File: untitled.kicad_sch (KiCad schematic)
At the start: 19 parts, among them J4 EURO_PWR, U2 AP2204K-3.3, U3 LM1117-5.0, U4 LM4040DBZ-5

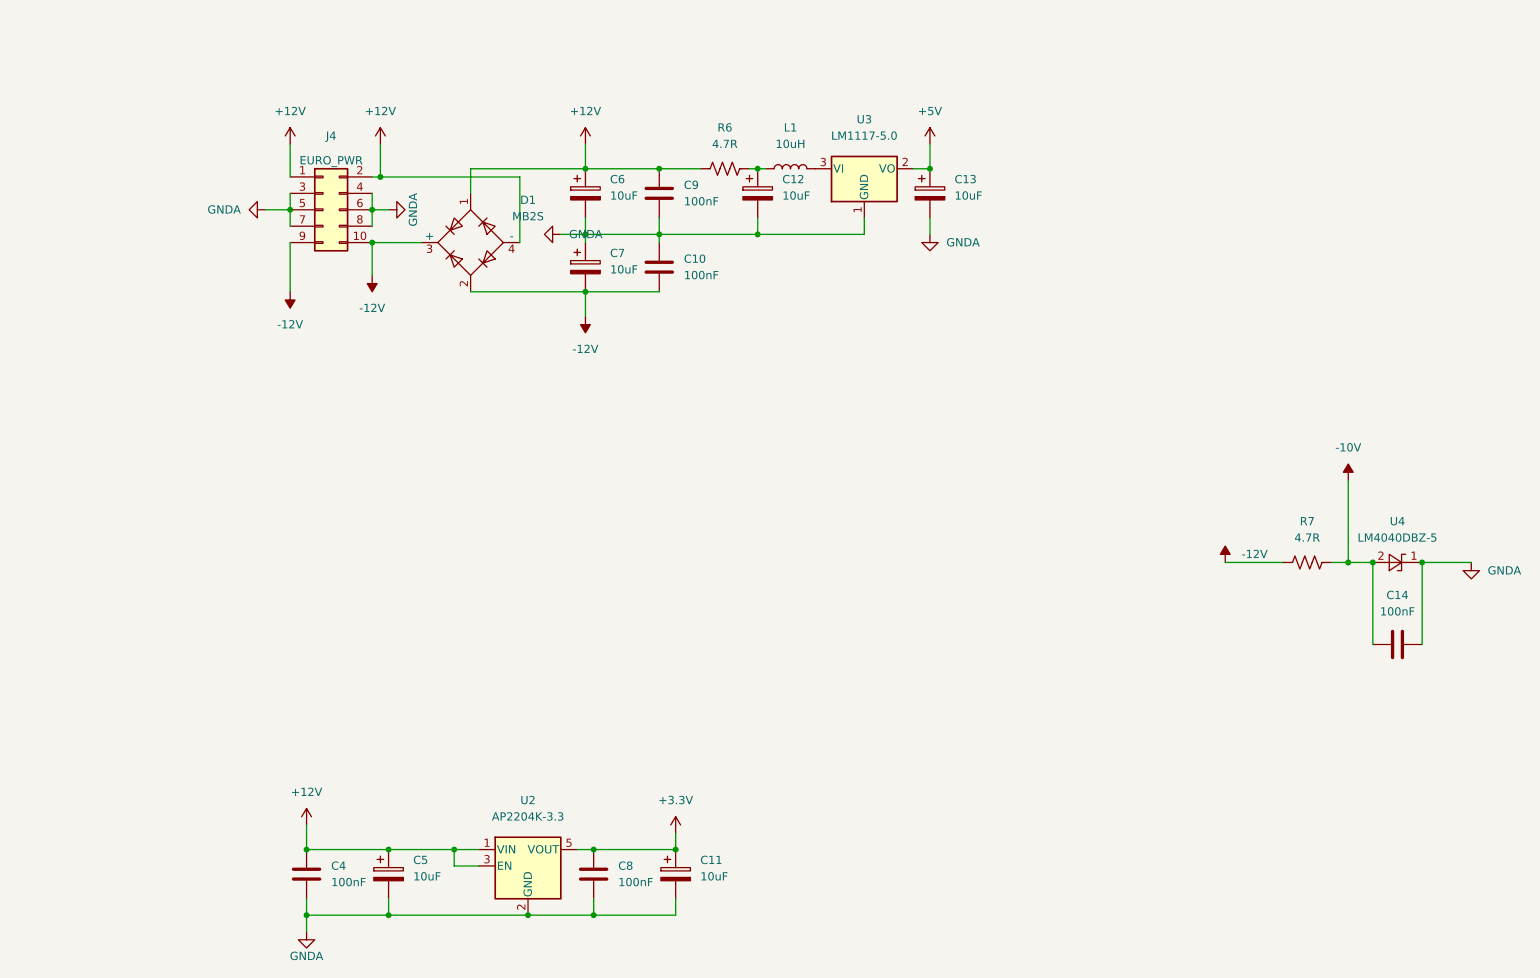
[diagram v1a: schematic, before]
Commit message: Version update
Added DC/DC power block and opAmps for audio input. Redesigned PCB completely moving all components to one side so that it can lay flat.
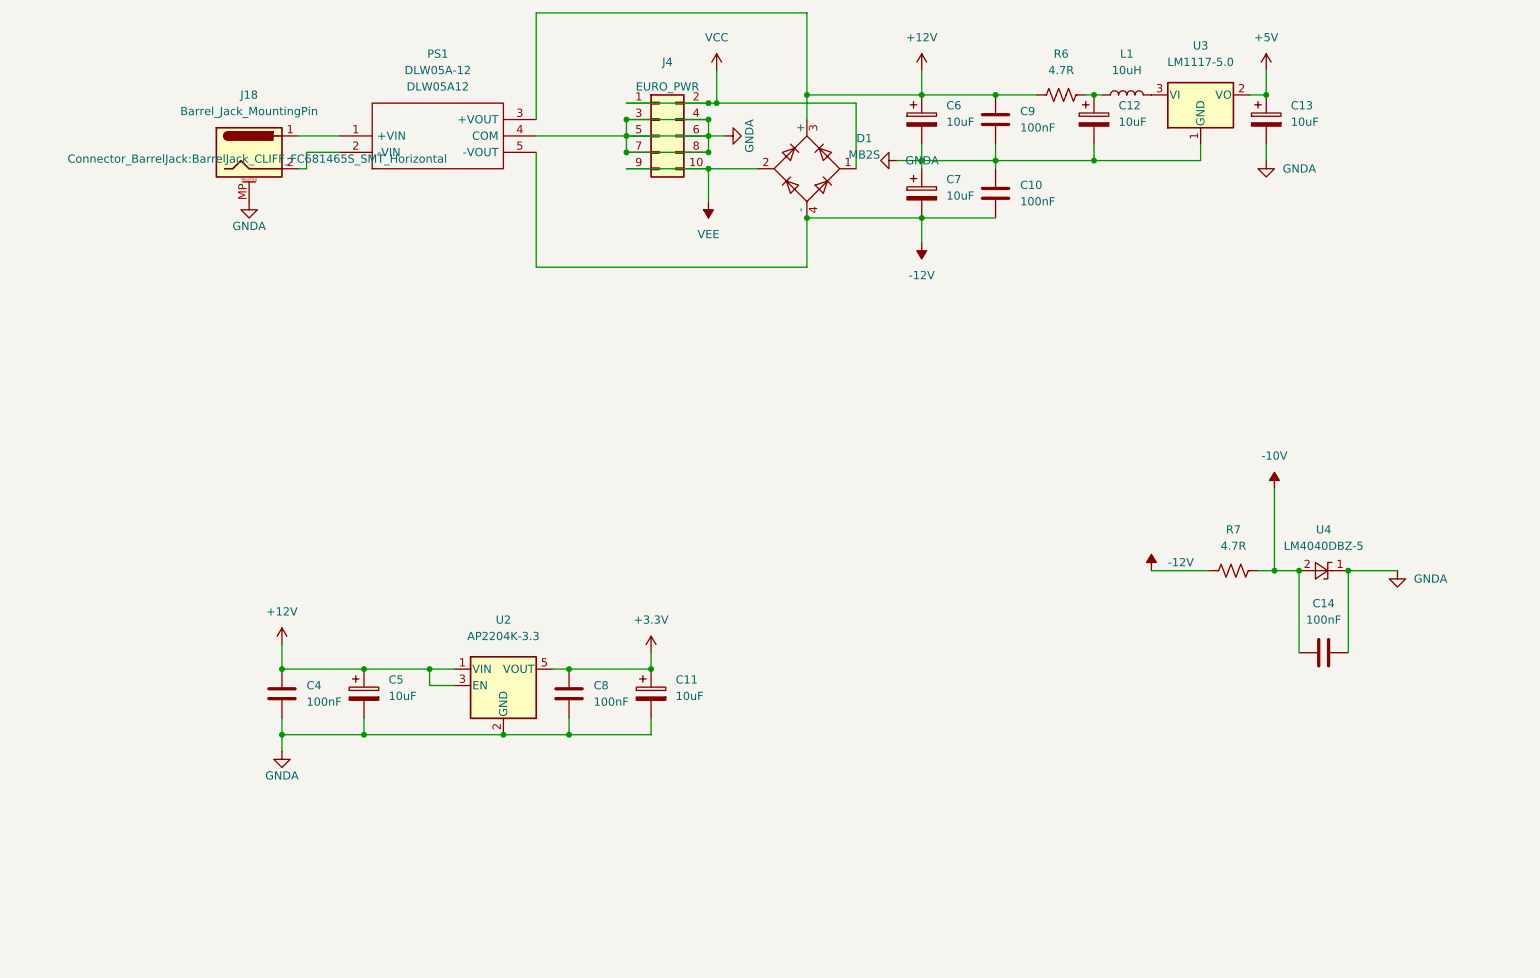
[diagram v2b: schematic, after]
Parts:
- added J18: Barrel_Jack_MountingPin, Connector_BarrelJack:BarrelJack_CLIFF_FC681465S_SMT_Horizontal, symbol Connector:Barrel_Jack_MountingPin
- added PS1: DLW05A-12, DLW05A12, symbol DLW05A-12:DLW05A-12
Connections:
- net +12V: now also D1.3 (+), PS1.3 (+VOUT); no longer D1.1, D1.4 (-), J4.1 (Pin_1), J4.2 (Pin_2)
- net -12V: now also D1.4 (-), PS1.5 (-VOUT); no longer D1.2, D1.3 (+), J4.10 (Pin_10), J4.9 (Pin_9)
- net GNDA: now also J18.MP (MountPin), PS1.4 (COM)
- new net: J18.1, PS1.1 (+VIN)
- new net: J18.2, PS1.2 (-VIN)
- new net VCC: D1.1, J4.1 (Pin_1), J4.2 (Pin_2)
- new net VEE: D1.2, J4.10 (Pin_10), J4.9 (Pin_9)
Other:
- moved on the sheet: C10, C11, C12, C13, C14, C4, C5, C6, C7, C8, C9, D1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
